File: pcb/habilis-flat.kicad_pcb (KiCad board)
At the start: 2 copper layers, 164 x 172.3 mm, 86 parts, among them SW1 MX, SW10 MX, SW11 MX, SW12 MX, SW13 MX, SW14 MX, SW15 MX, SW16 MX, SW17 MX, SW18 MX, SW19 MX, SW2 MX, SW20 MX, SW21 MX, SW22 MX, SW23 MX, SW24 MX, SW25 MX, SW26 MX, SW27 MX, SW28 MX, SW29 MX, SW3 MX, SW30 MX, SW31 MX, SW32 MX, SW33 MX, SW34 MX, SW35 MX, SW4 MX, SW5 MX, SW6 MX, SW7 MX, SW8 MX, SW9 MX, U1 ProMicro

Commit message: Simplify schematic, pacify ERC
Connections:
- net Net-(SW_RST1-Pad2) renamed GND

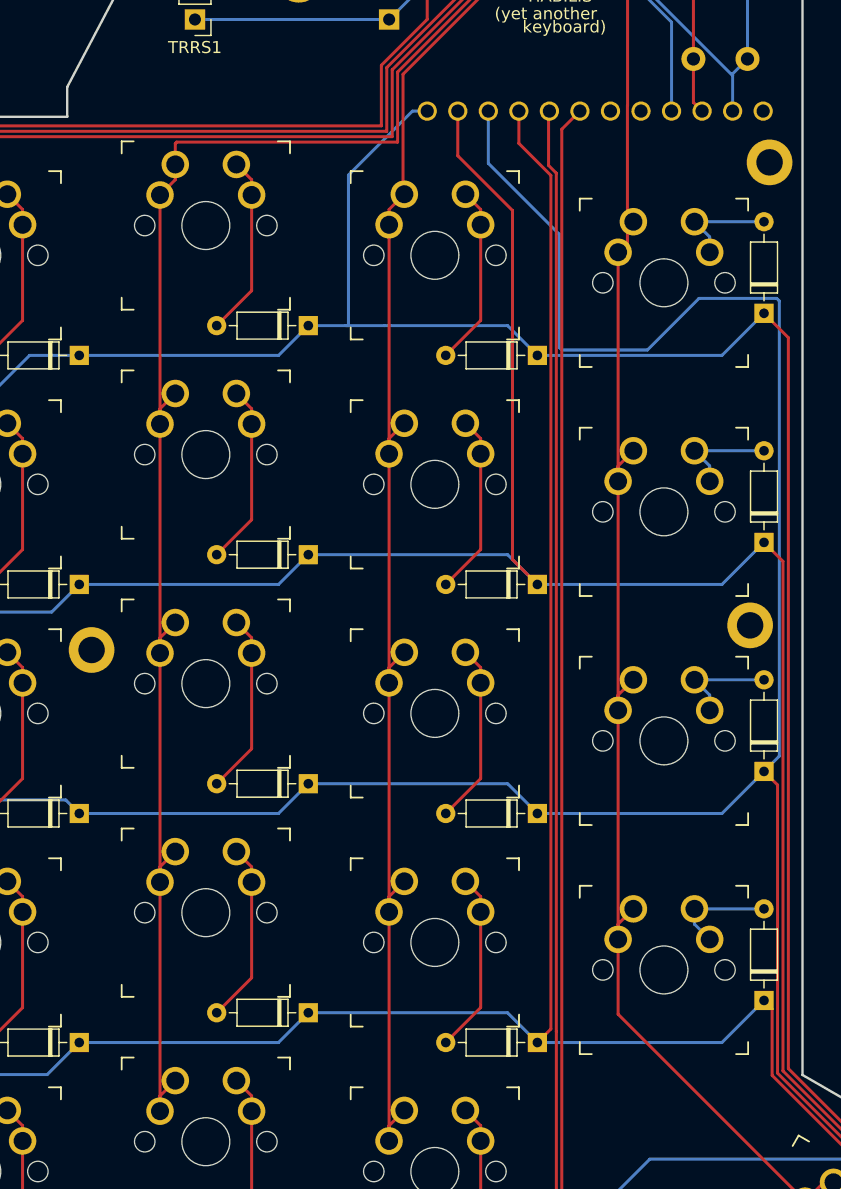
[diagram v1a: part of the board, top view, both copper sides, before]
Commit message: Add more mounting holes
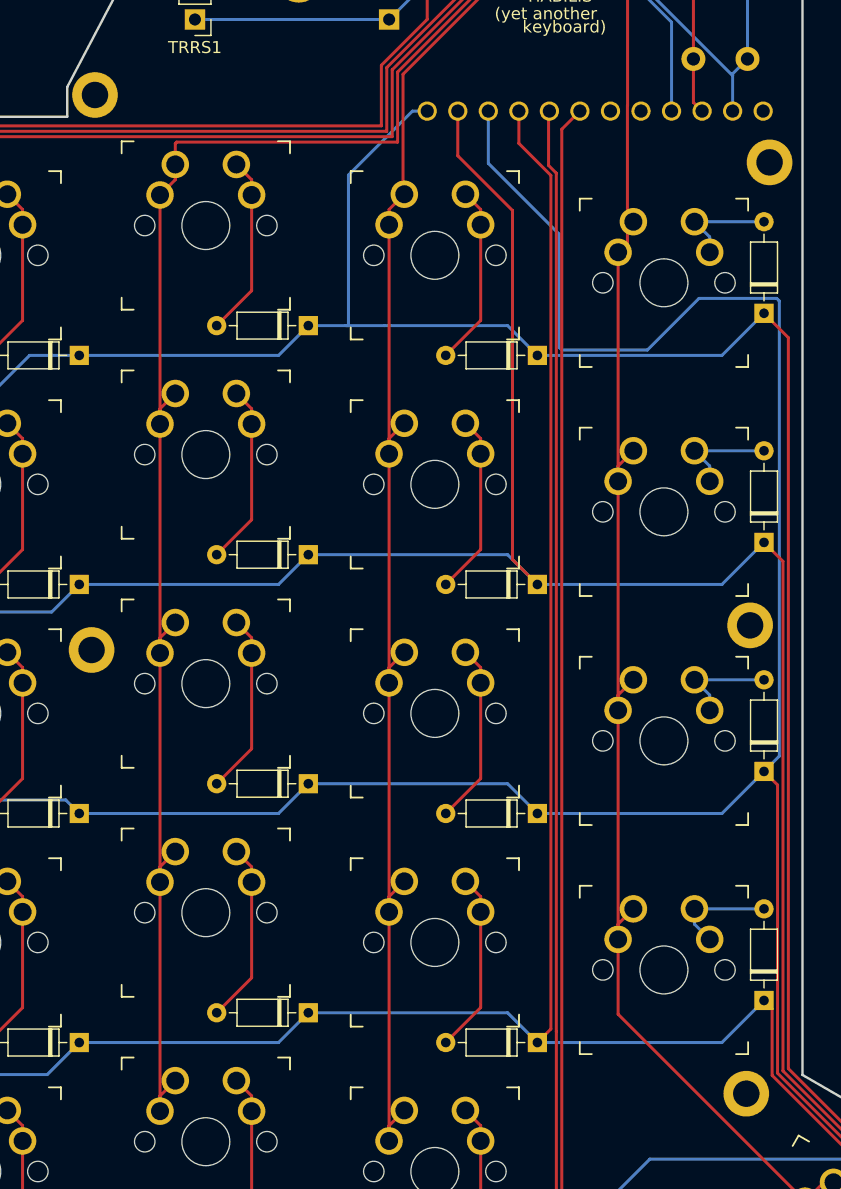
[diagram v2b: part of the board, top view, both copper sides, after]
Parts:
- added ?: MountingHole_2.2mm_M2_DIN965_Pad_NO_Silkscreem, project-components:MountingHole_2.2mm_M2_DIN965_Pad_NO_Silkscreem, F.Cu at (99.6, 70.0)
- added ?: MountingHole_2.2mm_M2_DIN965_Pad_NO_Silkscreem, project-components:MountingHole_2.2mm_M2_DIN965_Pad_NO_Silkscreem, F.Cu at (45.4, -13.0)
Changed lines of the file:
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@@
   )
   (footprint "project-components:MountingHole_2.2mm_M2_DIN965_Pad_NO_Silkscreem" (layer "F.Cu")
+    (at 99.559425 70.048903)
+    (descr "Mounting Hole 2.2mm, M2, DIN965")
+    (tags "mounting hole 2.2mm m2 din965")
+    (attr board_only exclude_from_pos_files exclude_from_bom)
+    (fp_text reference "" (at 0 -2.9) (layer "F.SilkS") hide
+        (effects (font (size 1 1) (thickness 0.15)))
+    )
+    (fp_text value "MountingHole_2.2mm_M2_DIN965_Pad_NO_Silkscreem" (at 0 2.9) (layer "F.Fab")
+        (effects (font (size 1 1) (thickness 0.15)))
+    )
+    (fp_text user "${REFERENCE}" (at 0 0) (layer "F.Fab")
+        (effects (font (size 1 1) (thickness 0.15)))
+    )
+    (fp_circle (center 0 0) (end 1.9 0)
+      (stroke (width 0.15) (type solid)) (fill none) (layer "Cmts.User"))
+    (fp_circle (center 0 0) (end 2.15 0)
+      (stroke (width 0.05) (type solid)) (fill none) (layer "F.CrtYd"))
+    (pad "1" thru_hole circle (at 0 0) (size 3.8 3.8) (drill 2.2) (layers "*.Cu" "*.Mask"))
+  )
+  (footprint "project-components:MountingHole_2.2mm_M2_DIN965_Pad_NO_Silkscreem" (layer "F.Cu")
     (at 90.510747 82.44347)
     (descr "Mounting Hole 2.2mm, M2, DIN965")
@@
     )
   )
+  (footprint "project-components:MountingHole_2.2mm_M2_DIN965_Pad_NO_Silkscreem" (layer "F.Cu")
+    (at 45.39084 -13.016885)
+    (descr "Mounting Hole 2.2mm, M2, DIN965")
+    (tags "mounting hole 2.2mm m2 din965")
+    (attr board_only exclude_from_pos_files exclude_from_bom)
+    (fp_text reference "" (at 0 -2.9) (layer "F.SilkS") hide
+        (effects (font (size 1 1) (thickness 0.15)))
+    )
+    (fp_text value "MountingHole_2.2mm_M2_DIN965_Pad_NO_Silkscreem" (at 0 2.9) (layer "F.Fab")
+        (effects (font (size 1 1) (thickness 0.15)))
+    )
+    (fp_text user "${REFERENCE}" (at 0 0) (layer "F.Fab")
+        (effects (font (size 1 1) (thickness 0.15)))
+    )
+    (fp_circle (center 0 0) (end 1.9 0)
+      (stroke (width 0.15) (type solid)) (fill none) (layer "Cmts.User"))
+    (fp_circle (center 0 0) (end 2.15 0)
+      (stroke (width 0.05) (type solid)) (fill none) (layer "F.CrtYd"))
+    (pad "1" thru_hole circle (at 0 0) (size 3.8 3.8) (drill 2.2) (layers "*.Cu" "*.Mask"))
+  )
   (footprint "project-components:D_DO-35_SOD27_P7.62mm_Horizontal" (layer "F.Cu")

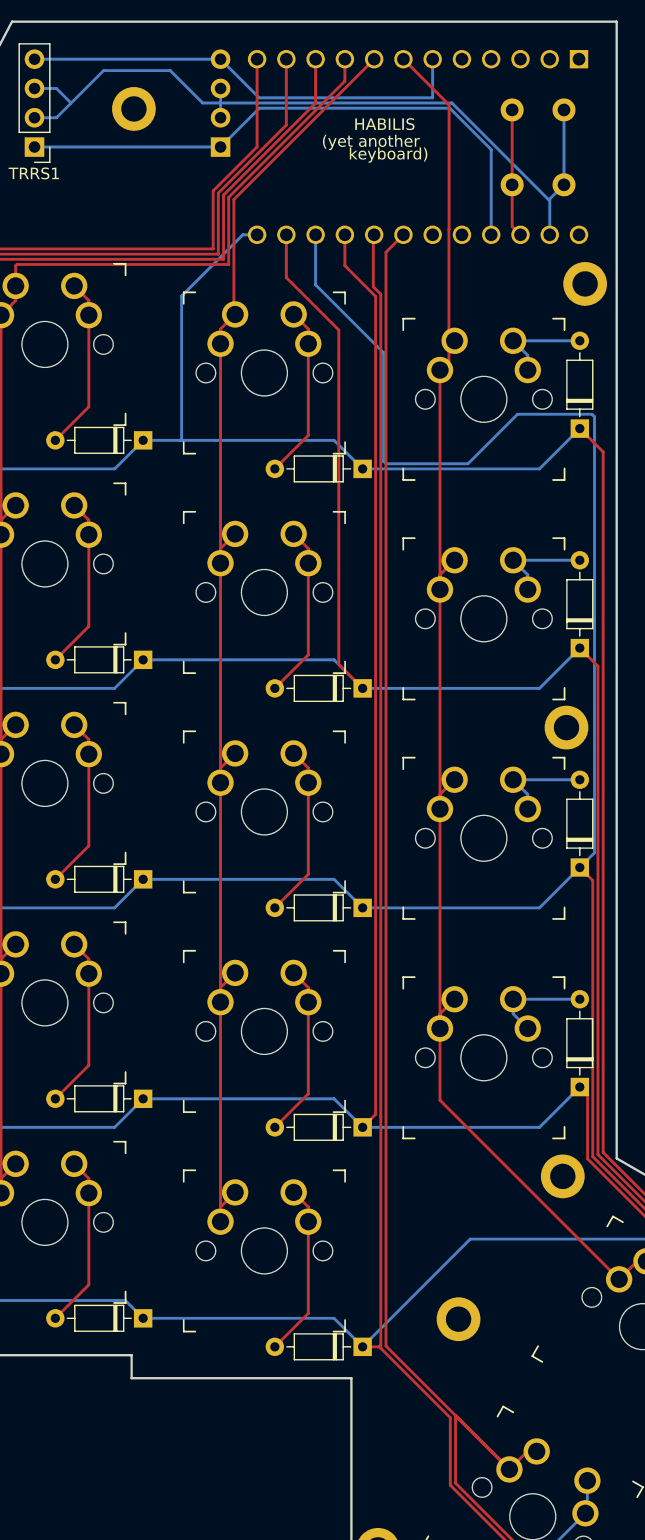
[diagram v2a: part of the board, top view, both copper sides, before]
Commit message: Replace reset button fp with one I have at hand
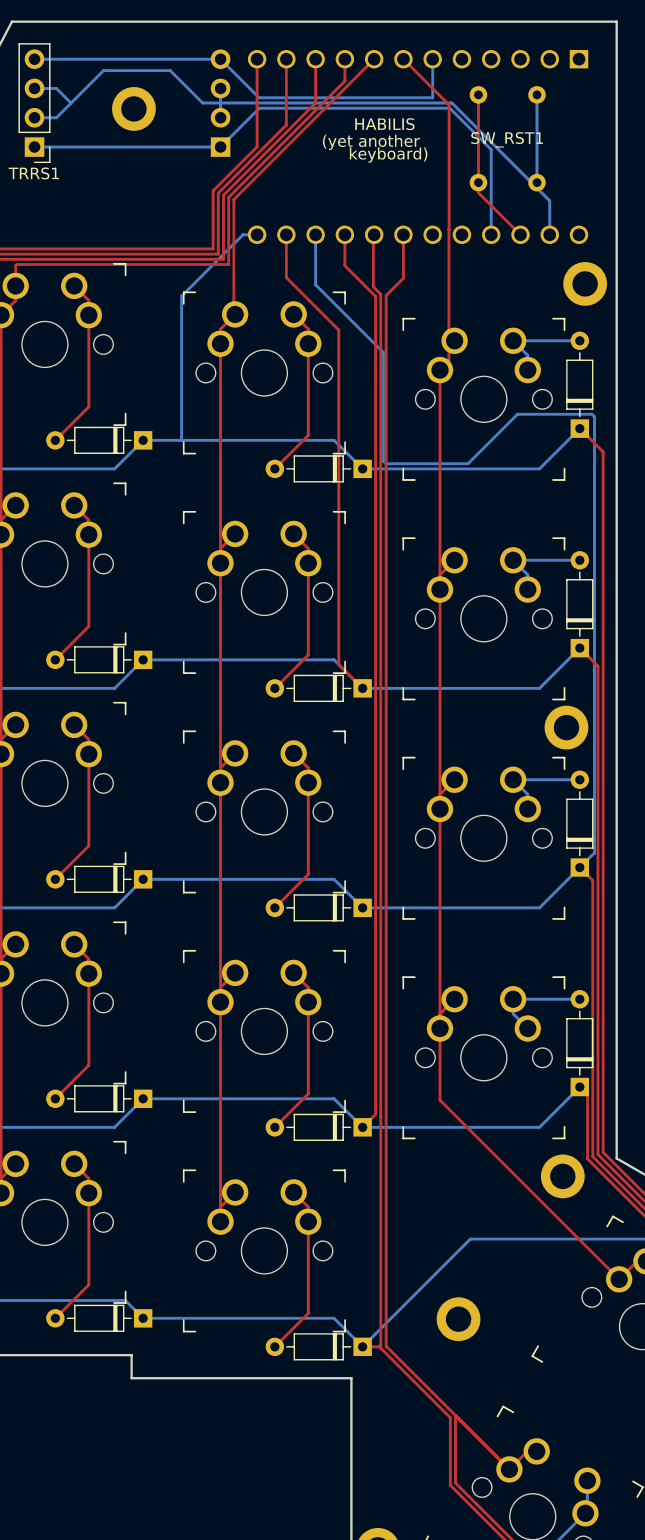
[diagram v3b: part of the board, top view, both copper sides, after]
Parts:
- SW_RST1: footprint Button_Switch_THT:SW_PUSH_6mm -> project-components:that_push_button_i_have_in_stock; moved to F.Cu
- moved SW_RST1 3.20 mm to (92.2, -23.8), turned to 0 degrees
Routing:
- net Net-(U1-RST): track 11.1 -> 13.7 mm
- net GND: track 68.7 -> 67.9 mm

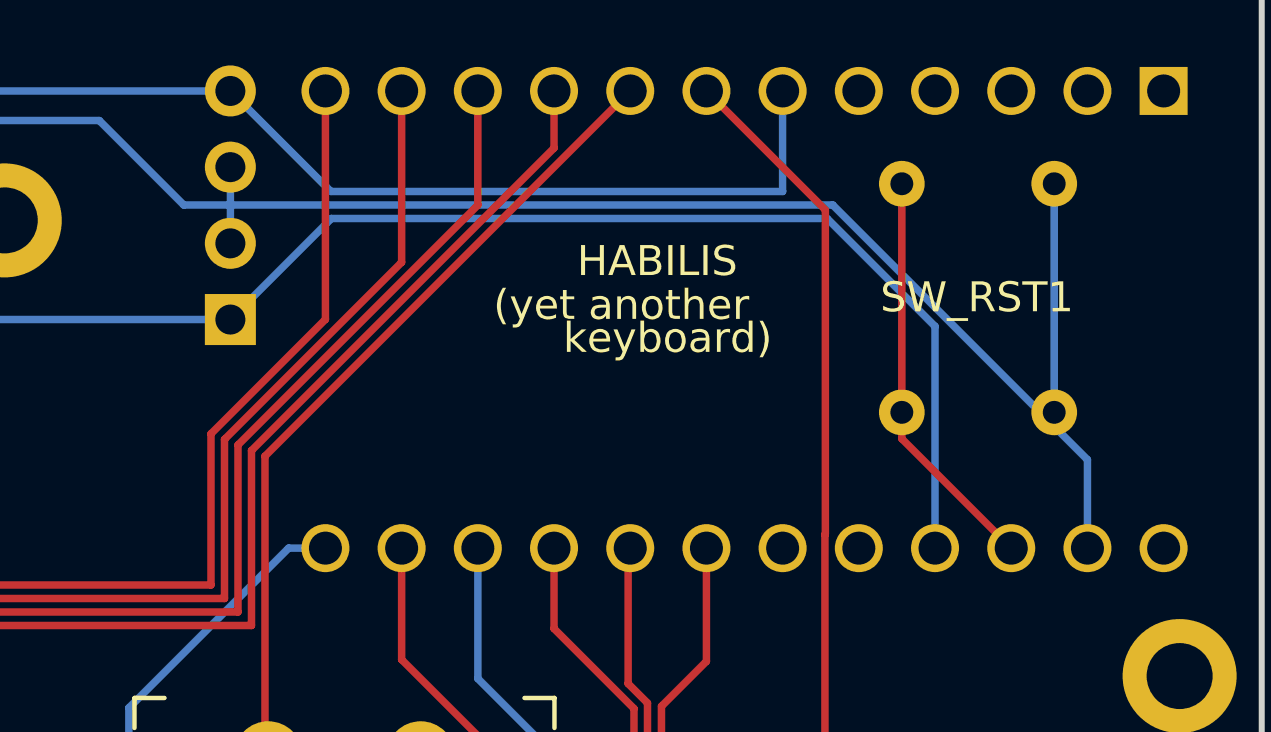
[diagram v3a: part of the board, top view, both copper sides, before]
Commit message: Fix footprint for reset button
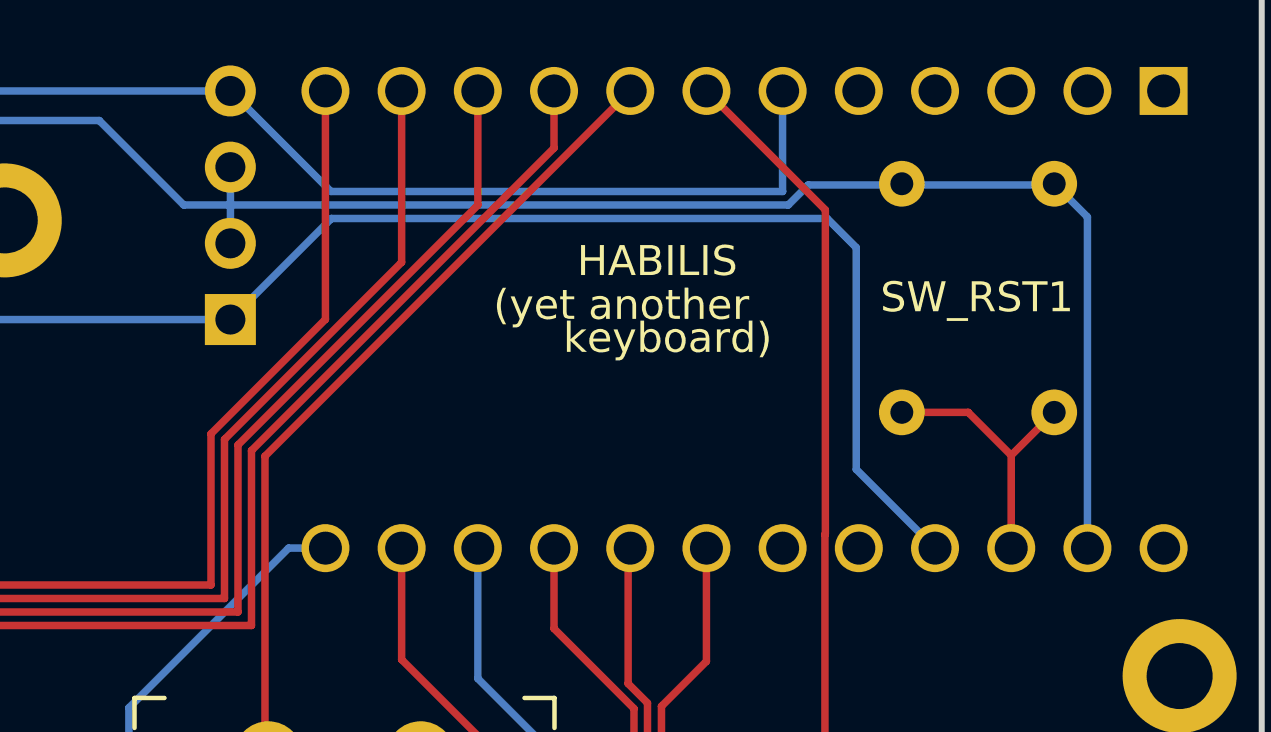
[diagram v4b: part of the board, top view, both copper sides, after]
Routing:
- net Net-(U1-RST): track 13.7 -> 9.36 mm
- net GND: track 67.9 -> 65.6 mm
